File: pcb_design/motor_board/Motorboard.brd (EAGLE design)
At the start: 31 x 31 mm, 79 parts, among them M1 STEPPER_MOTOR_SMD, M2 STEPPER_MOTOR_SMD

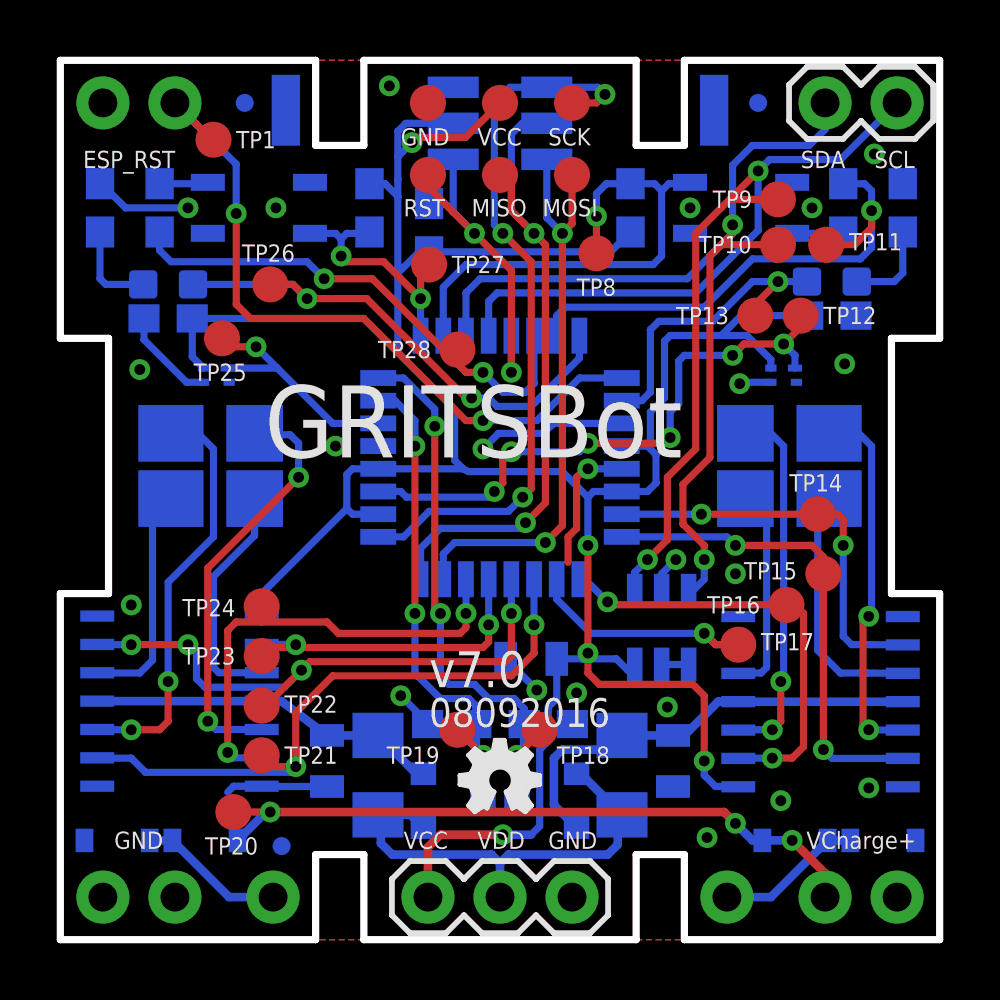
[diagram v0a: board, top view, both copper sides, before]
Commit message: Updated the GRITSBot's motor board
1. Added a reset pin so that the main board can reset
    the motor board.
2. Fixed the polarity of the current sensors.
3. Added test pins on the top layer.
4. Added castellated edges to mount motors mechanically
    more stable.
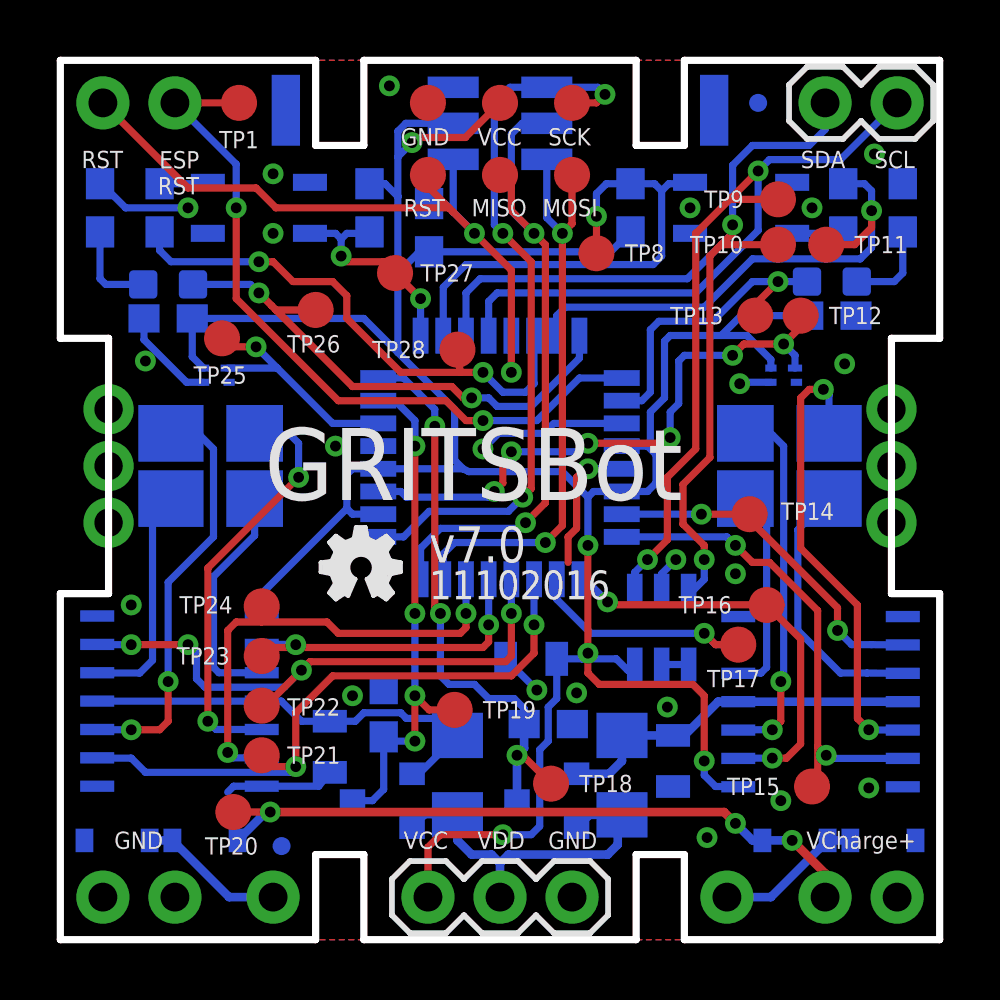
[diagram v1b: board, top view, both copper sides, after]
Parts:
- moved LOGO1 8.96 mm to (9.18, 12.0)
- moved TP15 7.51 mm to (26.5, 5.40)
- moved R4 2.80 mm to (14.0, 5.80), turned to 270 degrees
- moved R10 2.43 mm to (11.4, 8.00), turned to 270 degrees
- moved CUR_LEFT 2.40 mm to (11.4, 4.90), turned to 270 degrees
- moved TP14 2.40 mm to (24.3, 15.0)
- moved TP18 1.94 mm to (17.3, 5.50)
- moved TP26 1.84 mm to (9.00, 22.2)
- moved TP1 1.58 mm to (6.30, 29.5)
- moved TP27 1.24 mm to (11.8, 23.5)
- moved TP19 0.71 mm to (13.9, 8.10)
- moved TP16 0.70 mm to (24.9, 11.8)
- moved C1 0.51 mm to (9.50, 6.80)
- moved JP4 0.20 mm to (6.30, 29.5)
- turned R9 to 270 degrees
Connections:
- net RESET: now also JP_RST.1
- net VBAT: now also CUR_LEFT.2, CUR_RIGHT.2, R4.2, R9.2; no longer CUR_LEFT.1, CUR_RIGHT.1, R4.1, R9.1
- net VMOTOR_L: now also CUR_LEFT.1, R4.1; no longer CUR_LEFT.2, R4.2
- net VMOTOR_R: now also CUR_RIGHT.1, R9.1; no longer CUR_RIGHT.2, R9.2
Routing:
- net RESET: track 13.4 -> 27.1 mm
- net M2OUT3: track 13.5 -> 17.0 mm
- net VBAT: track 16.3 -> 13.0 mm
- net VMOTOR_L: track 12.5 -> 15.6 mm
- net VMOTOR_R: track 15.9 -> 13.1 mm
- net M2IN4: track 14.2 -> 12.4 mm
- net AD2_LINE_LEFT: track 8.99 -> 7.67 mm
- net GND: track 27.3 -> 26.2 mm, vias 22 -> 23
- net CURRENT_LEFT: track 17.8 -> 18.8 mm, vias 3 -> 4
- net LINE_LEFT: track 18.2 -> 19.1 mm
- net M2OUT4: track 8.85 -> 9.43 mm
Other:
- board text added: "11102016"
- board text added: "ESP RST"
- board text removed: "08092016"
- board text removed: "ESP_RST"

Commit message: Moved test points to allow for pogo pins on test board
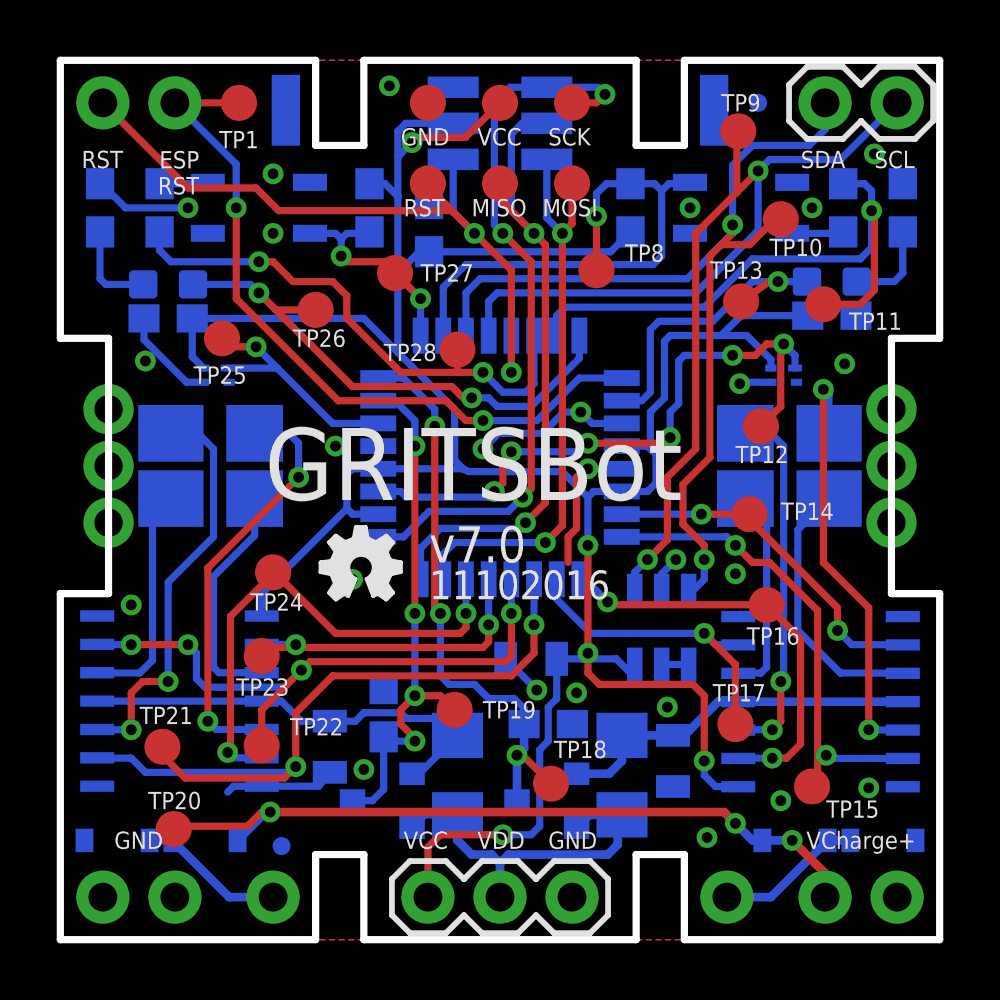
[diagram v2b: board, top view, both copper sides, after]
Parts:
- moved TP12 4.14 mm to (24.7, 18.1)
- moved TP21 3.51 mm to (3.60, 6.80)
- moved TP17 2.80 mm to (23.8, 7.60)
- moved TP9 2.78 mm to (23.9, 28.5)
- moved TP20 2.18 mm to (4.00, 3.90)
- moved TP11 2.10 mm to (26.9, 22.4)
- moved TP22 1.40 mm to (7.10, 6.85)
- moved TP24 1.26 mm to (7.50, 12.9)
- moved TP10 0.91 mm to (25.4, 25.4)
- moved TP13 0.71 mm to (24.0, 22.5)
- moved TP8 0.60 mm to (18.9, 23.6)
- moved TP5 0.30 mm to (13.0, 26.7)
- moved TP6 0.30 mm to (15.5, 26.7)
- moved TP7 0.30 mm to (18.0, 26.7)
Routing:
- net M1IN4: track 22.4 -> 26.6 mm
- net LINE_RIGHT: track 18.4 -> 20.8 mm
- net VCHRG: track 24.2 -> 26.5 mm
- net M2IN2: track 9.14 -> 11.4 mm
- net TEMP_RIGHT: track 20.9 -> 23.0 mm
- net M1IN2: track 16.6 -> 17.8 mm
- net M1IN3: track 21.0 -> 22.1 mm
- net M2OUT3: track 17.0 -> 16.0 mm
- net AD3_LINE_RIGHT: track 17.9 -> 18.5 mm
- net A5_SCL: track 38.0 -> 38.5 mm
- net GND: track 26.2 -> 26.6 mm, vias 23 -> 25

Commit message: Removed reverse polarity protection on charge input
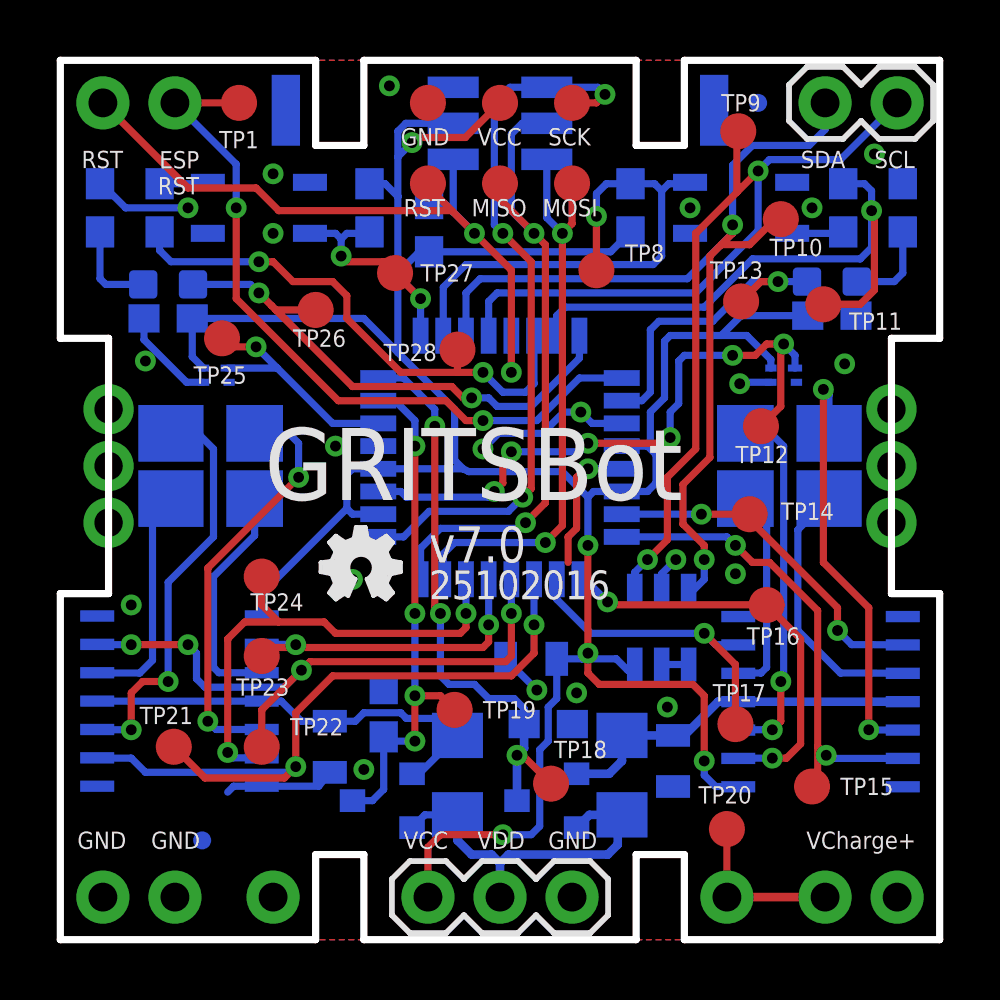
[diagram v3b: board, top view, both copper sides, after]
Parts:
- removed D1, D2, D3, D4: BAT20J, SparkFun-DiscreteSemi:SOD-323
- moved TP20 19.5 mm to (23.5, 3.90)
- moved JP5 2.81 mm to (5.00, 3.50)
- moved TP24 0.43 mm to (7.10, 12.8)
- moved TP21 0.40 mm to (4.00, 6.80)
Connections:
- removed net PAD_LEFT: D1.C, D2.A, JP_CHRG_L.1
- removed net PAD_RIGHT: D3.C, D4.A, JP_CHRG_R.1
- net GND: now also JP_CHRG_L.1; no longer D1.A, D3.A
- net VCHRG: now also JP_CHRG_R.1; no longer D2.C, D4.C
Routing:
- net VCHRG: track 26.5 -> 5.86 mm, vias 3 -> 0
- net PAD_RIGHT: track 5.18 -> 0.00 mm
- net PAD_LEFT: track 5.18 -> 0.00 mm
- net M1IN2: track 17.8 -> 18.9 mm
- net GND: vias 25 -> 22
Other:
- board text added: "25102016"
- board text removed: "11102016"

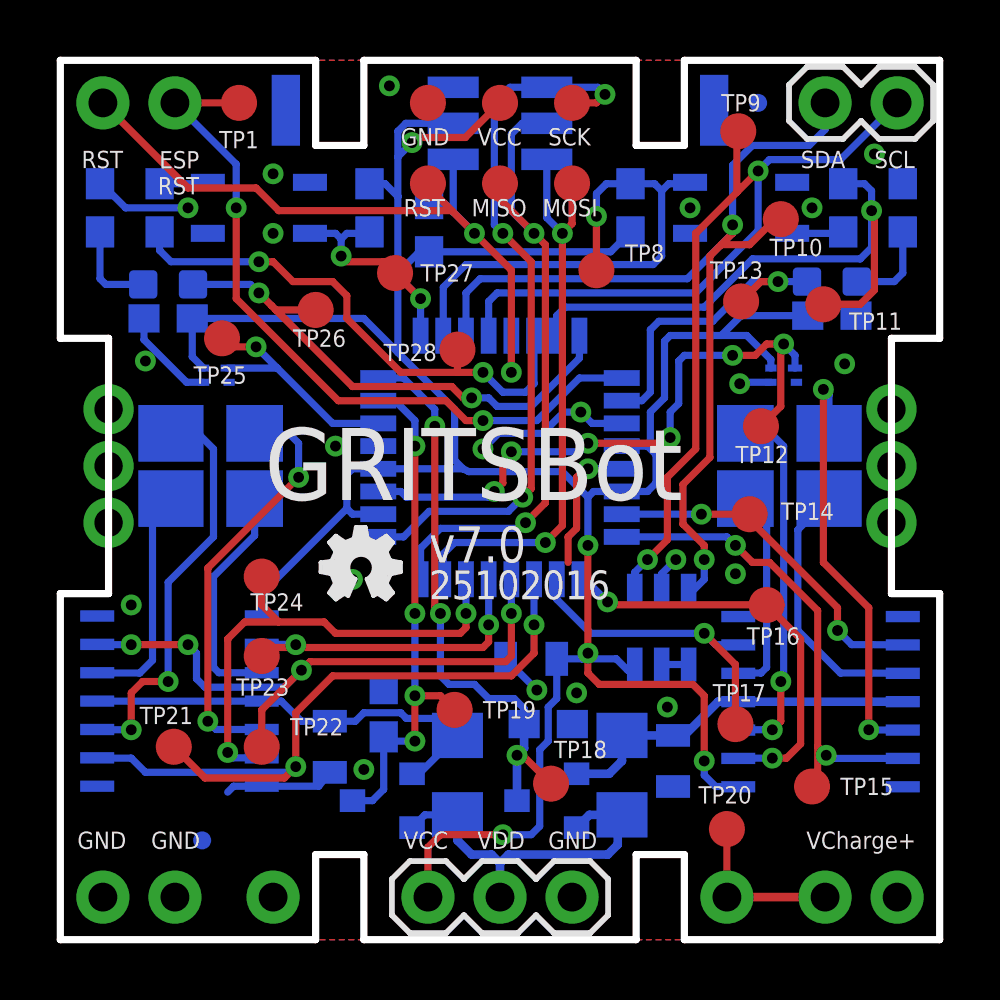
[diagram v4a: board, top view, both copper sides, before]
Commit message: Changed LED color value on motor board
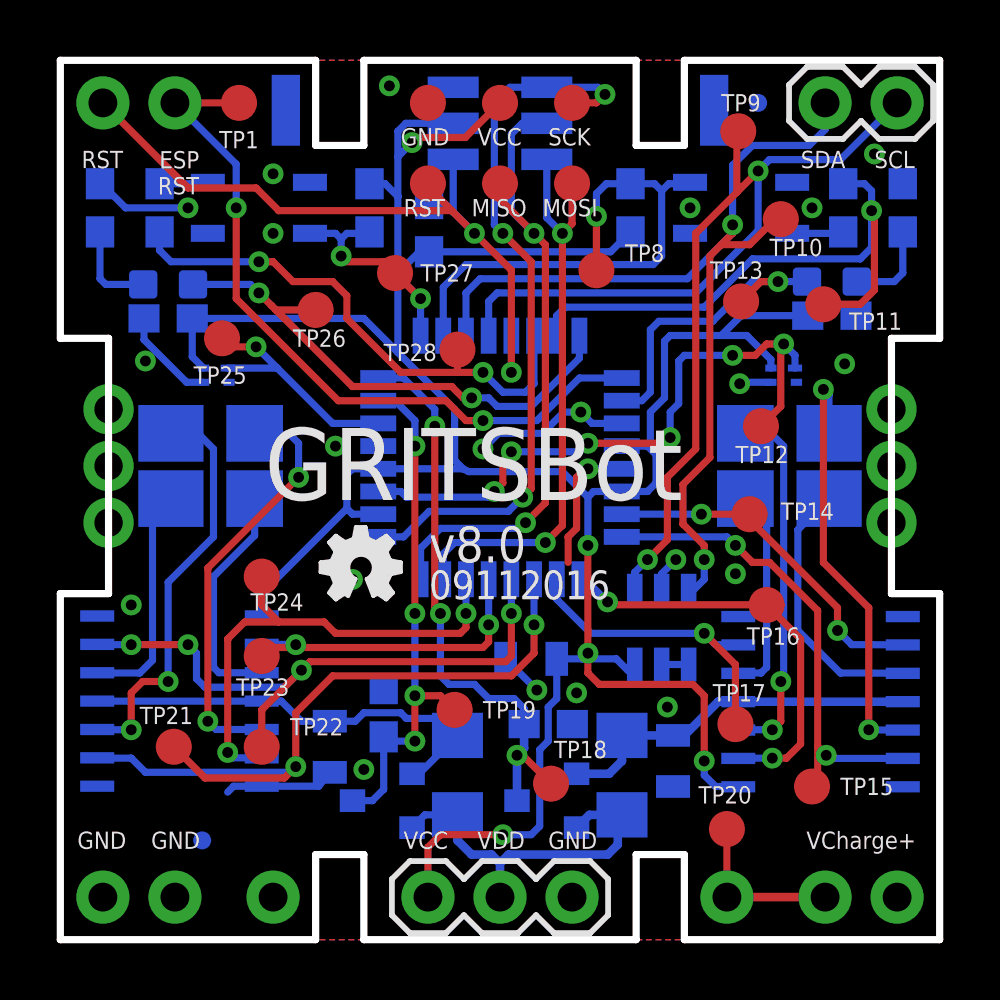
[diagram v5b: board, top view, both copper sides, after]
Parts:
- LED_LEFT, LED_RIGHT: value red -> green
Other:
- board text added: "09112016"
- board text added: "v8.0"
- board text removed: "25102016"
- board text removed: "v7.0"
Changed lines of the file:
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@@
 <text x="12.1" y="3.2" size="0.6096" layer="21">VCC</text>
 <text x="7.2" y="15.5" size="2.54" layer="21">GRITSBot</text>
-<text x="13" y="13.3" size="1.27" layer="21">v7.0</text>
-<text x="13" y="12" size="1.016" layer="21">25102016</text>
+<text x="13" y="13.3" size="1.27" layer="21">v8.0</text>
+<text x="13" y="12" size="1.016" layer="21">09112016</text>
 <text x="23.1" y="26.5" size="0.6096" layer="22" rot="MR180">QRE
 1113</text>
@@
 </element>
 <element name="ATMEGA168P" library="GRITSBot" package="TQFP32-08" value="ATMEGA168" x="15.5" y="17" smashed="yes" rot="MR0"/>
-<element name="LED_RIGHT" library="SparkFun-LED" package="LED-0603" value="red" x="27.2" y="23.2" smashed="yes" rot="MR90"/>
+<element name="LED_RIGHT" library="SparkFun-LED" package="LED-0603" value="green" x="27.2" y="23.2" smashed="yes" rot="MR90"/>
 <element name="R1" library="SparkFun-Resistors" package="0603" value="1k" x="29.7" y="25.8" smashed="yes" rot="MR270">
 <attribute name="PROD_ID" value="RES-08306" x="22.08" y="44.4436" size="1.778" layer="28" rot="MR270" display="off"/>
@@
 <element name="JP_GND" library="SparkFun-Connectors" package="1X02_NO_SILK" value="M021X02_NO_SILK" x="1.5" y="1.5" smashed="yes"/>
 <element name="JP_PROG" library="GRITSBot" package="3X2_SMD_HEADER" value="3X2_SMD_HEADER" x="15.5" y="28.8" smashed="yes" rot="MR180"/>
-<element name="LED_LEFT" library="SparkFun-LED" package="LED-0603" value="red" x="3.8" y="23.1" smashed="yes" rot="MR270">
+<element name="LED_LEFT" library="SparkFun-LED" package="LED-0603" value="green" x="3.8" y="23.1" smashed="yes" rot="MR270">
 <attribute name="VALUE" x="4.816" y="22.0205" size="0.4064" layer="28" rot="MR0"/>
 </element>
